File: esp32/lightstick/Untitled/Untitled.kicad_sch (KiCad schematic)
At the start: 10 parts, among them J1 Conn_02x09_Odd_Even, J2 Conn_01x04_Pin, J3 Conn_01x02_Pin, J4 Conn_01x02_Pin, J5 Conn_01x08_Pin, J6 Conn_01x08_Pin, J7 Conn_01x08_Pin, Q1 S8050

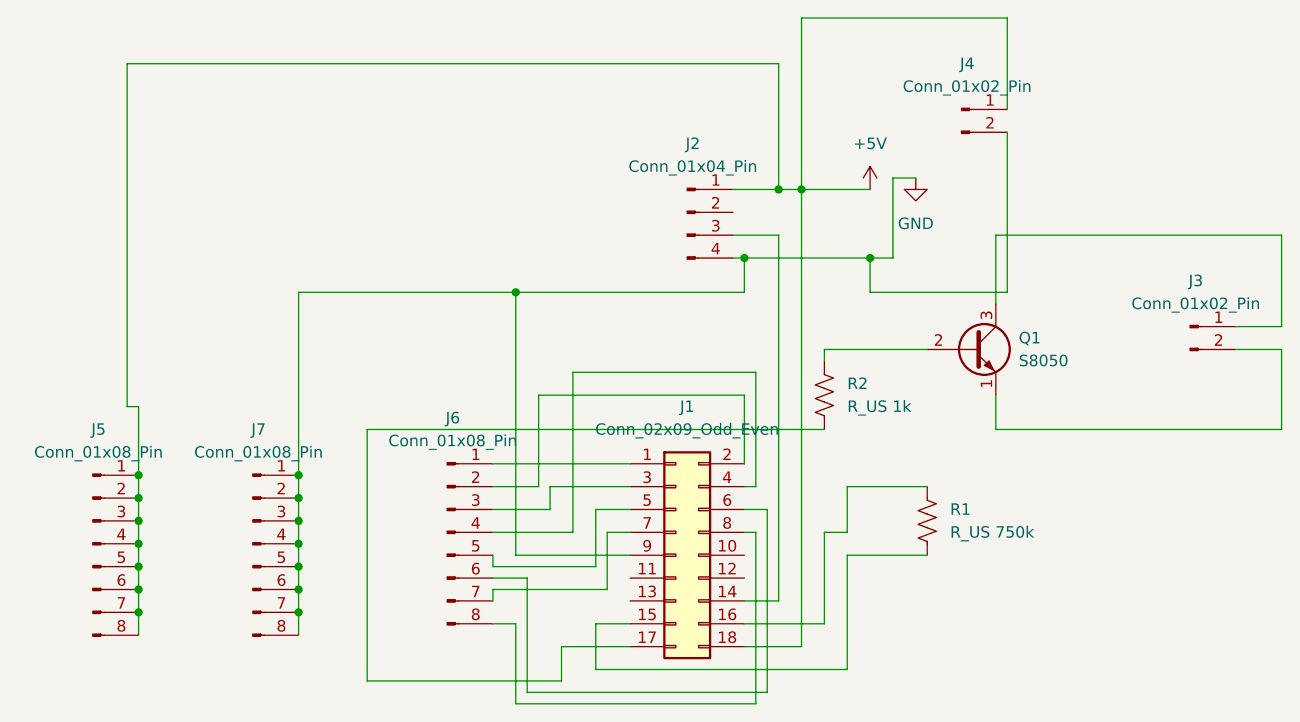
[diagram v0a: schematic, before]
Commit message: update schematic
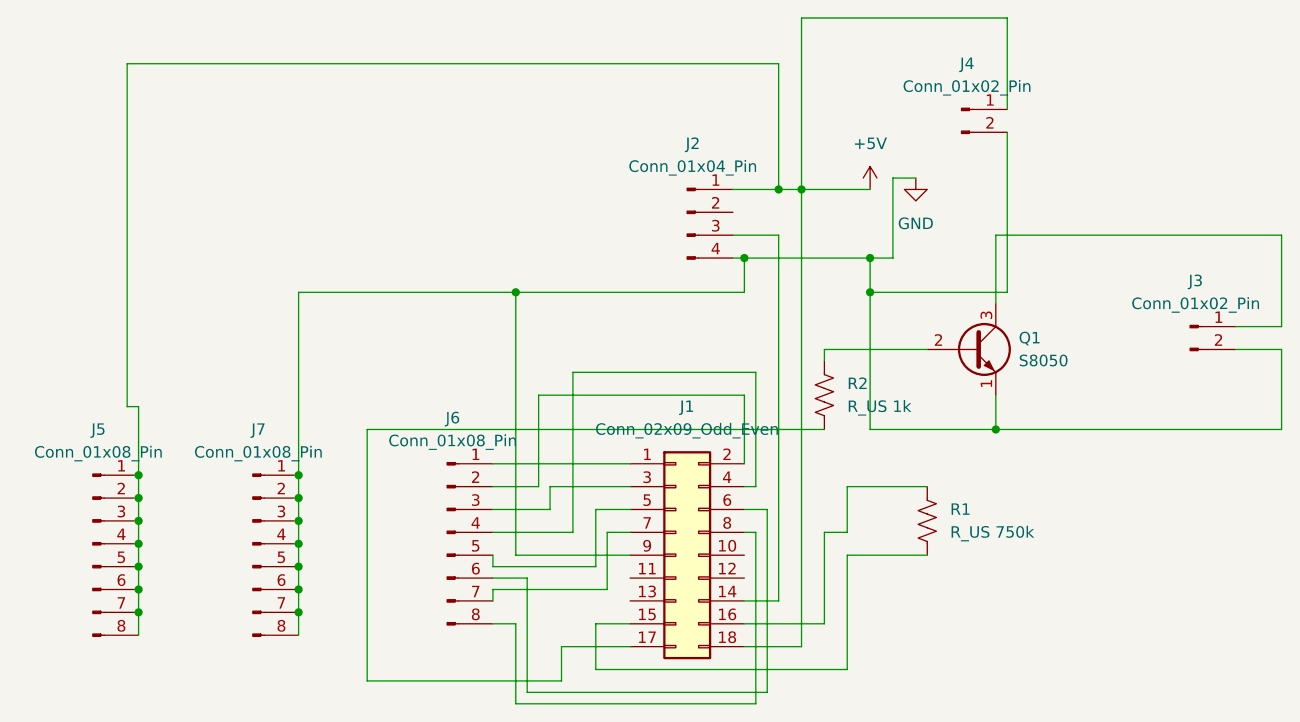
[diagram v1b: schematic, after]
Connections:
- net GND: now also J3.2 (Pin_2), Q1.1 (E)
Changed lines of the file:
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@@
+	)
+	(junction
+		(at 102.87 57.15)
+		(diameter 0)
+		(color 0 0 0 0)
 	)
 	(junction
@@
 	)
 	(junction
+		(at 116.84 72.39)
+		(diameter 0)
+		(color 0 0 0 0)
+	)
+	(junction
 		(at 39.37 87.63)
 		(diameter 0)
@@
 	(wire
 		(pts
+			(xy 102.87 72.39) (xy 116.84 72.39)
+		)
+		(stroke
+			(width 0)
+			(type default)
+		)
+	)
+	(wire
+		(pts
 			(xy 97.79 93.98) (xy 88.9 93.98)
 		)
@@
 	(wire
 		(pts
+			(xy 102.87 57.15) (xy 118.11 57.15)
+		)
+		(stroke
+			(width 0)
+			(type default)
+		)
+	)
+	(wire
+		(pts
 			(xy 87.63 50.8) (xy 92.71 50.8)
 		)
@@
 	(wire
 		(pts
-			(xy 118.11 57.15) (xy 102.87 57.15)
-		)
-		(stroke
-			(width 0)
-			(type default)
-		)
-	)
-	(wire
-		(pts
 			(xy 88.9 96.52) (xy 95.25 96.52)
 		)
@@
 		)
 		(stroke
+			(width 0)
+			(type default)
+		)
+	)
+	(wire
+		(pts
+			(xy 102.87 72.39) (xy 102.87 57.15)
+		)
+		(stroke
